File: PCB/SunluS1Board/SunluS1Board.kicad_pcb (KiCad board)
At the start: 2 copper layers, 48.2 x 57 mm, 45 parts, among them J1 Conn_01x14, J2 aNTC, J3 hNTC, J4 Fan, J5 HT, J6 Power, J7 Conn_02x03_Counter_Clockwise, Q1 AO3400A, Q2 AO3400A, Q3 AO3400A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

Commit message: continue PCB
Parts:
- J7: value Conn_02x03_Counter_Clockwise -> Conn_02x03_Odd_Even
- Q1: value AO3400A -> SIA440DJ-T1-GE3; footprint Package_TO_SOT_SMD:SOT-23 -> easyeda2kicad:SC-70-6L_L2.0-W2.0-P0.65-BL
- SW1, SW2: moved to B.Cu
- moved C1 167.1 mm to (28.5, 46.6)
- moved C10 167.1 mm to (38.8, 75.0)
- moved C13 167.1 mm to (32.5, 54.1)
- moved C14 167.1 mm to (32.5, 56.6)
- moved C2 167.1 mm to (28.5, 49.1)
- moved C3 167.1 mm to (28.5, 51.6)
- moved C4 167.1 mm to (28.5, 54.1)
- moved C9 167.1 mm to (32.5, 46.6)
- moved D1 167.1 mm to (39.1, 32.1)
- moved R12 167.1 mm to (40.6, 51.6)
- moved R4 167.1 mm to (36.5, 49.1)
- moved D2 144.6 mm to (78.1, 39.5), turned to 180 degrees
- moved SW2 137.4 mm to (75.5, 68.1)
- moved R8 136.2 mm to (66.9, 64.7), turned to -90 degrees
- moved R13 135.8 mm to (78.1, 37.4)
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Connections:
- J7 pad 1: GND -> NRST
- J7 pad 3: +3.3V -> SWCLK
- J7 pad 4: SWDIO -> GND
- J7 pad 5: SWCLK -> SWDIO
- J7 pad 6: NRST -> +3.3V
- Q1 pad 1: Net-(Q1-G) -> hCon
- Q1 pad 2: GND -> hCon
- Q1 pad 3: hCon -> Net-(Q1-G)
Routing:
- net GND: track 0.00 -> 0.90 mm
- added copper zone on F.Cu, net GND

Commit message: update footprint
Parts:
- C13, C4, C8: footprint Capacitor_SMD:C_0603_1608Metric -> Capacitor_SMD:C_0805_2012Metric
- moved C2 76.3 mm to (102.8, 66.5)
- moved R6 64.0 mm to (78.0, 61.5), turned to 90 degrees
- moved R5 61.1 mm to (78.0, 65.0), turned to 90 degrees
- moved C1 59.9 mm to (85.0, 66.5)
- moved Q2 45.0 mm to (81.4, 65.1)
- moved C10 13.9 mm to (31.0, 63.5)
- moved U1 6.82 mm to (83.0, 54.5), turned to 90 degrees

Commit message: placement done
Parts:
- moved D3 99.9 mm to (98.9, 51.5)
- moved C6 95.0 mm to (102.4, 54.4), turned to -90 degrees
- moved C8 92.4 mm to (92.4, 54.8), turned to -90 degrees
- moved C7 90.0 mm to (94.4, 54.8), turned to -90 degrees
- moved U2 87.8 mm to (97.5, 54.9), turned to -90 degrees
- moved C5 83.8 mm to (100.4, 54.5), turned to -90 degrees
- moved C9 72.1 mm to (102.9, 62.3)
- moved C10 71.9 mm to (102.9, 64.1)
- moved D1 54.7 mm to (88.0, 56.6), turned to -90 degrees
- moved C3 54.3 mm to (82.3, 59.5)
- moved C4 54.3 mm to (82.3, 61.5)
- moved R4 51.6 mm to (88.0, 53.0), turned to -90 degrees
- moved R12 45.3 mm to (85.0, 60.5), turned to 90 degrees
- moved C13 45.2 mm to (77.1, 46.7), turned to -90 degrees
- moved R2 44.9 mm to (86.5, 60.5), turned to 90 degrees
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
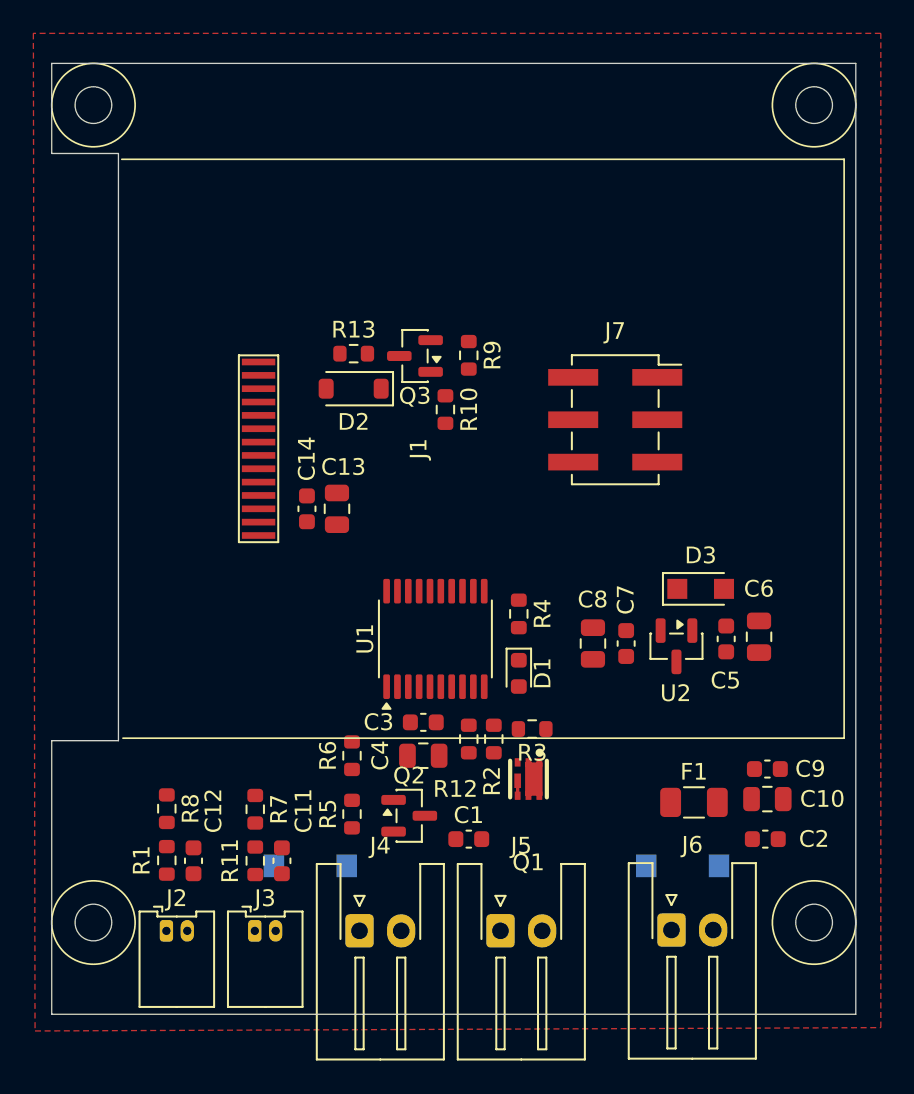
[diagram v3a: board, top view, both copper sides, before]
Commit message: mostly routed
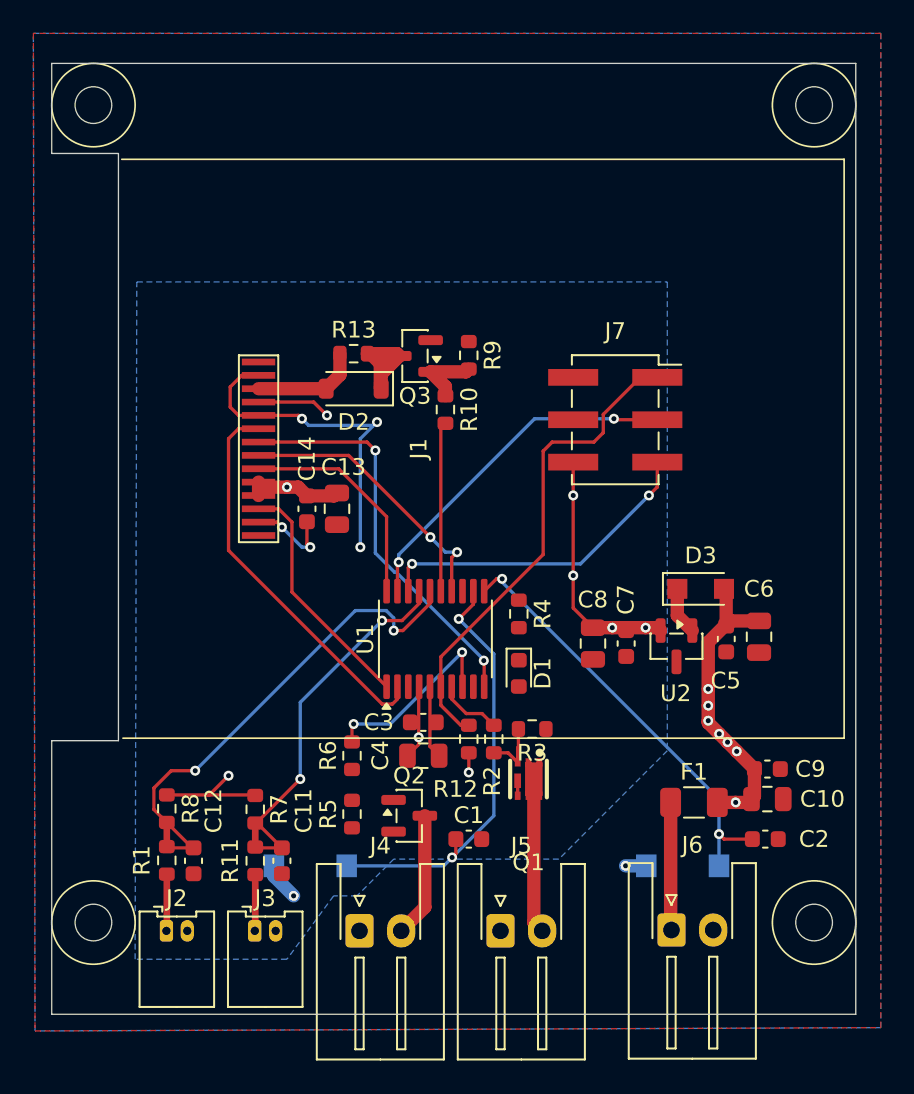
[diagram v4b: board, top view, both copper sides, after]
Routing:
- net +3.3V: track 0.00 -> 37.6 mm, vias 0 -> 9
- net GND: track 0.90 -> 34.6 mm, vias 0 -> 7
- net airNTC: track 0.00 -> 31.0 mm, vias 0 -> 2
- net NRST: track 0.00 -> 29.3 mm
- net B1: track 0.00 -> 26.1 mm, vias 0 -> 2
- net B2: track 0.00 -> 26.0 mm, vias 0 -> 2
- net A0: track 0.00 -> 24.1 mm, vias 0 -> 2
- net heatNTC: track 0.00 -> 24.0 mm, vias 0 -> 2
- net RET: track 0.00 -> 23.5 mm
- net SWCLK: track 0.00 -> 21.1 mm, vias 0 -> 2
- net SWDIO: track 0.00 -> 19.8 mm, vias 0 -> 2
- net +24V: track 0.00 -> 18.6 mm, vias 0 -> 7
- net MOSI: track 0.00 -> 16.8 mm, vias 0 -> 2
- net CS: track 0.00 -> 14.5 mm
- net SCK: track 0.00 -> 13.3 mm
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- added copper zone on B.Cu, net +24V
- added copper zone on B.Cu, net +3.3V
